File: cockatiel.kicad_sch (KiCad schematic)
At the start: 44 parts

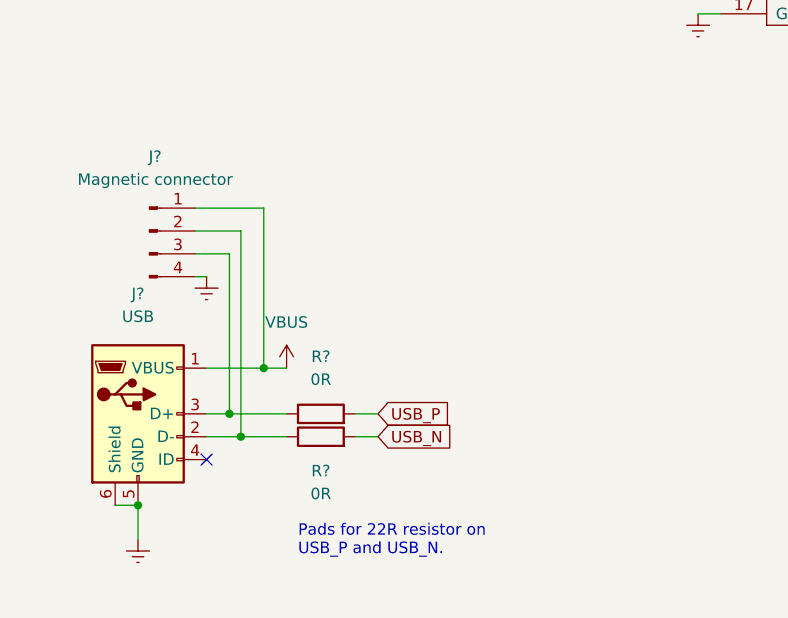
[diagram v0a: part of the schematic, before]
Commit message: Split the USB D+/D- lines using resistors.
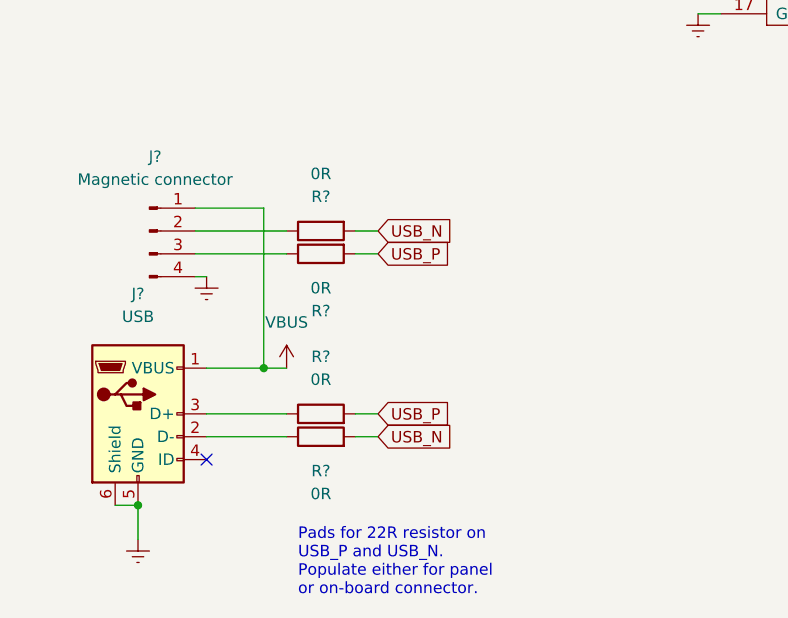
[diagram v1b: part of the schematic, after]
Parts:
- added R? (x2): 0R, Resistor_SMD:R_0805_2012Metric_Pad1.20x1.40mm_HandSolder, symbol Device:R
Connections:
- net USB_N: now also R?.2
- net USB_P: now also R?.2
- net at J?.3 (D+), R?.1: no longer J?.3 (Pin_3)
- net at J?.2 (D-), R?.1: no longer J?.2 (Pin_2)
- new net: J?.2 (Pin_2), R?.1
- new net: J?.3 (Pin_3), R?.1
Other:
- note added: "Pads for 22R resistor on USB_P and USB_N. Populate either for panel or on-board connector."
- note removed: "Pads for 22R resistor on USB_P and USB_N."
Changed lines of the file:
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@@
   (junction (at 212.09 121.92) (diameter 0) (color 0 0 0 0)
   )
-  (junction (at 38.1 176.53) (diameter 0) (color 0 0 0 0)
-  )
   (junction (at 219.71 121.92) (diameter 0) (color 0 0 0 0)
   )
@@
   )
   (junction (at 142.24 186.69) (diameter 0) (color 0 0 0 0)
-  )
-  (junction (at 36.83 173.99) (diameter 0) (color 0 0 0 0)
   )
   (junction (at 142.24 163.83) (diameter 0) (color 0 0 0 0)
@@
     (stroke (width 0) (type default) (color 0 0 0 0))
   )
+  (wire (pts (xy 33.02 153.67) (xy 43.18 153.67))
+    (stroke (width 0) (type default) (color 0 0 0 0))
+  )
   (wire (pts (xy 76.2 52.07) (xy 77.47 52.07))
     (stroke (width 0) (type default) (color 0 0 0 0))
@@
     (stroke (width 0) (type default) (color 0 0 0 0))
   )
+  (wire (pts (xy 50.8 156.21) (xy 53.34 156.21))
+    (stroke (width 0) (type default) (color 0 0 0 0))
+  )
   (wire (pts (xy 211.455 34.925) (xy 211.455 32.385))
     (stroke (width 0) (type default) (color 0 0 0 0))
@@
     (stroke (width 0) (type default) (color 0 0 0 0))
   )
-  (wire (pts (xy 36.83 173.99) (xy 43.18 173.99))
+  (wire (pts (xy 34.29 173.99) (xy 43.18 173.99))
     (stroke (width 0) (type default) (color 0 0 0 0))
   )
@@
     (stroke (width 0) (type default) (color 0 0 0 0))
   )
+  (wire (pts (xy 33.02 156.21) (xy 43.18 156.21))
+    (stroke (width 0) (type default) (color 0 0 0 0))
+  )
   (wire (pts (xy 201.295 34.925) (xy 208.915 34.925))
     (stroke (width 0) (type default) (color 0 0 0 0))
@@
     (stroke (width 0) (type default) (color 0 0 0 0))
   )
+  (wire (pts (xy 50.8 153.67) (xy 53.34 153.67))
+    (stroke (width 0) (type default) (color 0 0 0 0))
+  )
   (wire (pts (xy 235.585 34.925) (xy 235.585 21.59))
     (stroke (width 0) (type default) (color 0 0 0 0))
@@
     (stroke (width 0) (type default) (color 0 0 0 0))
   )
-  (wire (pts (xy 34.29 176.53) (xy 38.1 176.53))
-    (stroke (width 0) (type default) (color 0 0 0 0))
-  )
   (wire (pts (xy 69.85 116.84) (xy 91.44 116.84))
     (stroke (width 0) (type default) (color 0 0 0 0))
@@
     (stroke (width 0) (type default) (color 0 0 0 0))
   )
-  (wire (pts (xy 38.1 176.53) (xy 43.18 176.53))
+  (wire (pts (xy 34.29 176.53) (xy 43.18 176.53))
     (stroke (width 0) (type default) (color 0 0 0 0))
   )
@@
     (stroke (width 0) (type default) (color 0 0 0 0))
   )
-  (wire (pts (xy 33.02 153.67) (xy 38.1 153.67))
-    (stroke (width 0) (type default) (color 0 0 0 0))
-  )
   (wire (pts (xy 267.97 121.92) (xy 267.97 130.81))
     (stroke (width 0) (type default) (color 0 0 0 0))
@@
     (stroke (width 0) (type default) (color 0 0 0 0))
   )
-  (wire (pts (xy 34.29 173.99) (xy 36.83 173.99))
-    (stroke (width 0) (type default) (color 0 0 0 0))
-  )
   (wire (pts (xy 102.87 39.37) (xy 101.6 39.37))
     (stroke (width 0) (type default) (color 0 0 0 0))
@@
     (stroke (width 0) (type default) (color 0 0 0 0))
   )
-  (wire (pts (xy 36.83 156.21) (xy 36.83 173.99))
-    (stroke (width 0) (type default) (color 0 0 0 0))
-  )
   (wire (pts (xy 121.92 189.23) (xy 128.27 189.23))
     (stroke (width 0) (type default) (color 0 0 0 0))
@@
     (stroke (width 0) (type default) (color 0 0 0 0))
   )
-  (wire (pts (xy 33.02 156.21) (xy 36.83 156.21))
-    (stroke (width 0) (type default) (color 0 0 0 0))
-  )
   (wire (pts (xy 143.51 166.37) (xy 146.05 166.37))
     (stroke (width 0) (type default) (color 0 0 0 0))
@@
     (stroke (width 0) (type default) (color 0 0 0 0))
   )
-  (wire (pts (xy 38.1 153.67) (xy 38.1 176.53))
-    (stroke (width 0) (type default) (color 0 0 0 0))
-  )
   (wire (pts (xy 30.48 119.38) (xy 36.83 119.38))
     (stroke (width 0) (type default) (color 0 0 0 0))
@@
     (stroke (width 0) (type default) (color 0 0 0 0))
   )
-  (text "Pads for 22R resistor on \nUSB_P and USB_N." (at 44.45 189.865 0)
+  (text "Pads for 22R resistor on \nUSB_P and USB_N.\nPopulate either for panel\nor on-board connector."
+    (at 44.45 194.31 0)
     (effects (font (size 1.27 1.27)) (justify left bottom))
   )
@@
     )
   )
+  (global_label "USB_N" (shape input) (at 53.34 153.67 0) (fields_autoplaced)
+    (effects (font (size 1.27 1.27)) (justify left))
+    (property "Intersheet References" "${INTERSHEET_REFS}" (id 0) (at 61.8612 153.5906 0)
+      (effects (font (size 1.27 1.27)) (justify left) hide)
+    )
+  )
   (global_label "BT_UART_RX" (shape input) (at 88.9 114.3 180) (fields_autoplaced)
     (effects (font (size 1.27 1.27)) (justify right))
@@
     (property "Intersheet References" "${INTERSHEET_REFS}" (id 0) (at 75.4802 111.6806 0)
       (effects (font (size 1.27 1.27)) (justify right) hide)
+    )
+  )
+  (global_label "USB_P" (shape input) (at 53.34 156.21 0) (fields_autoplaced)
+    (effects (font (size 1.27 1.27)) (justify left))
+    (property "Intersheet References" "${INTERSHEET_REFS}" (id 0) (at 61.8007 156.1306 0)
+      (effects (font (size 1.27 1.27)) (justify left) hide)
     )
   )
@@
     (pin "1")
   )
+  (symbol (lib_id "Device:R") (at 46.99 153.67 90) (mirror x) (unit 1)
+    (in_bom yes) (on_board yes) (fields_autoplaced)
+    (property "Reference" "R?" (id 0) (at 46.99 149.86 90))
+    (property "Value" "0R" (id 1) (at 46.99 147.32 90))
+    (property "Footprint" "Resistor_SMD:R_0805_2012Metric_Pad1.20x1.40mm_HandSolder" (id 2) (at 46.99 151.892 90)
+      (effects (font (size 1.27 1.27)) hide)
+    )
+    (property "Datasheet" "~" (id 3) (at 46.99 153.67 0)
+      (effects (font (size 1.27 1.27)) hide)
+    )
+    (pin "1")
+    (pin "2")
+  )
   (symbol (lib_id "power:Earth") (at 146.05 166.37 0) (unit 1)
     (in_bom yes) (on_board yes) (fields_autoplaced)
@@
     )
     (pin "1")
+  )
+  (symbol (lib_id "Device:R") (at 46.99 156.21 90) (mirror x) (unit 1)
+    (in_bom yes) (on_board yes) (fields_autoplaced)
+    (property "Reference" "R?" (id 0) (at 46.99 162.56 90))
+    (property "Value" "0R" (id 1) (at 46.99 160.02 90))
+    (property "Footprint" "Resistor_SMD:R_0805_2012Metric_Pad1.20x1.40mm_HandSolder" (id 2) (at 46.99 154.432 90)
+      (effects (font (size 1.27 1.27)) hide)
+    )
+    (property "Datasheet" "~" (id 3) (at 46.99 156.21 0)
+      (effects (font (size 1.27 1.27)) hide)
+    )
+    (pin "1")
+    (pin "2")
   )
   (symbol (lib_id "Device:R") (at 82.55 53.34 0) (unit 1)
@@
       (reference "R?") (unit 1) (value "330") (footprint "Resistor_SMD:R_0805_2012Metric_Pad1.20x1.40mm_HandSolder")
     )
+    (path "/8bef48da-1a77-4708-80d6-e40ce0804d8b"
+      (reference "R?") (unit 1) (value "0R") (footprint "Resistor_SMD:R_0805_2012Metric_Pad1.20x1.40mm_HandSolder")
+    )
     (path "/984a861b-f6fe-4e48-b308-c05544ae2128"
       (reference "R?") (unit 1) (value "2K2") (footprint "")
@@
       (reference "R?") (unit 1) (value "330") (footprint "Resistor_SMD:R_0805_2012Metric_Pad1.20x1.40mm_HandSolder")
     )
+    (path "/b804d89b-7db6-4577-a13e-be600d5ceaab"
+      (reference "R?") (unit 1) (value "0R") (footprint "Resistor_SMD:R_0805_2012Metric_Pad1.20x1.40mm_HandSolder")
+    )
     (path "/bb6848f3-ae47-41fd-84f7-dda98b97154e"

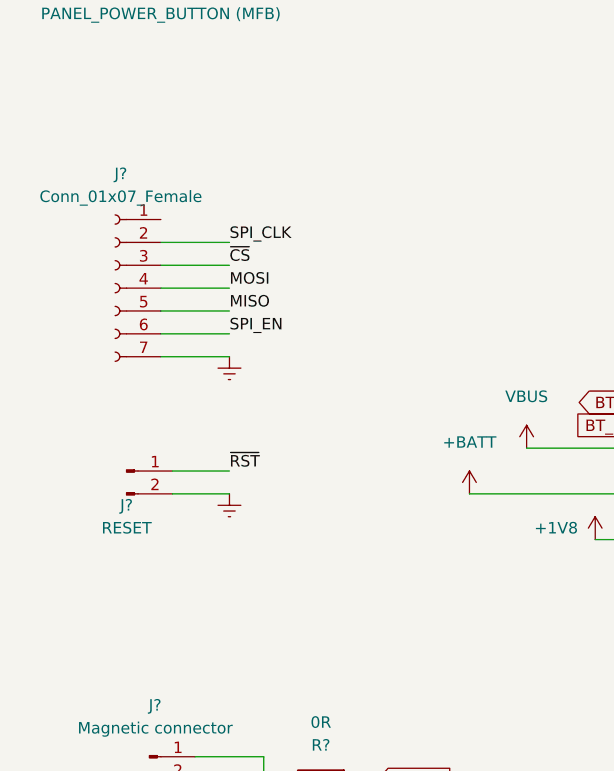
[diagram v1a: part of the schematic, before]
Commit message: Bring out the debug UART to a jumper
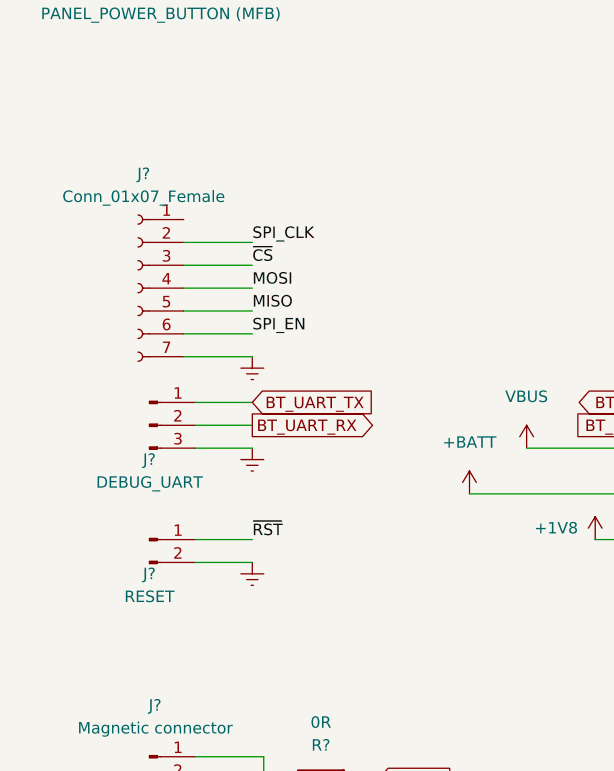
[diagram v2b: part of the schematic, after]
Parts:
- added J?: DEBUG_UART, Connector_PinHeader_2.54mm:PinHeader_1x03_P2.54mm_Vertical, symbol Connector:Conn_01x03_Male
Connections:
- net BT_UART_RX: now also J?.2 (Pin_2)
- net BT_UART_TX: now also J?.1 (Pin_1)
- net Earth: now also J?.3 (Pin_3)
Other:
- moved on the sheet: J?

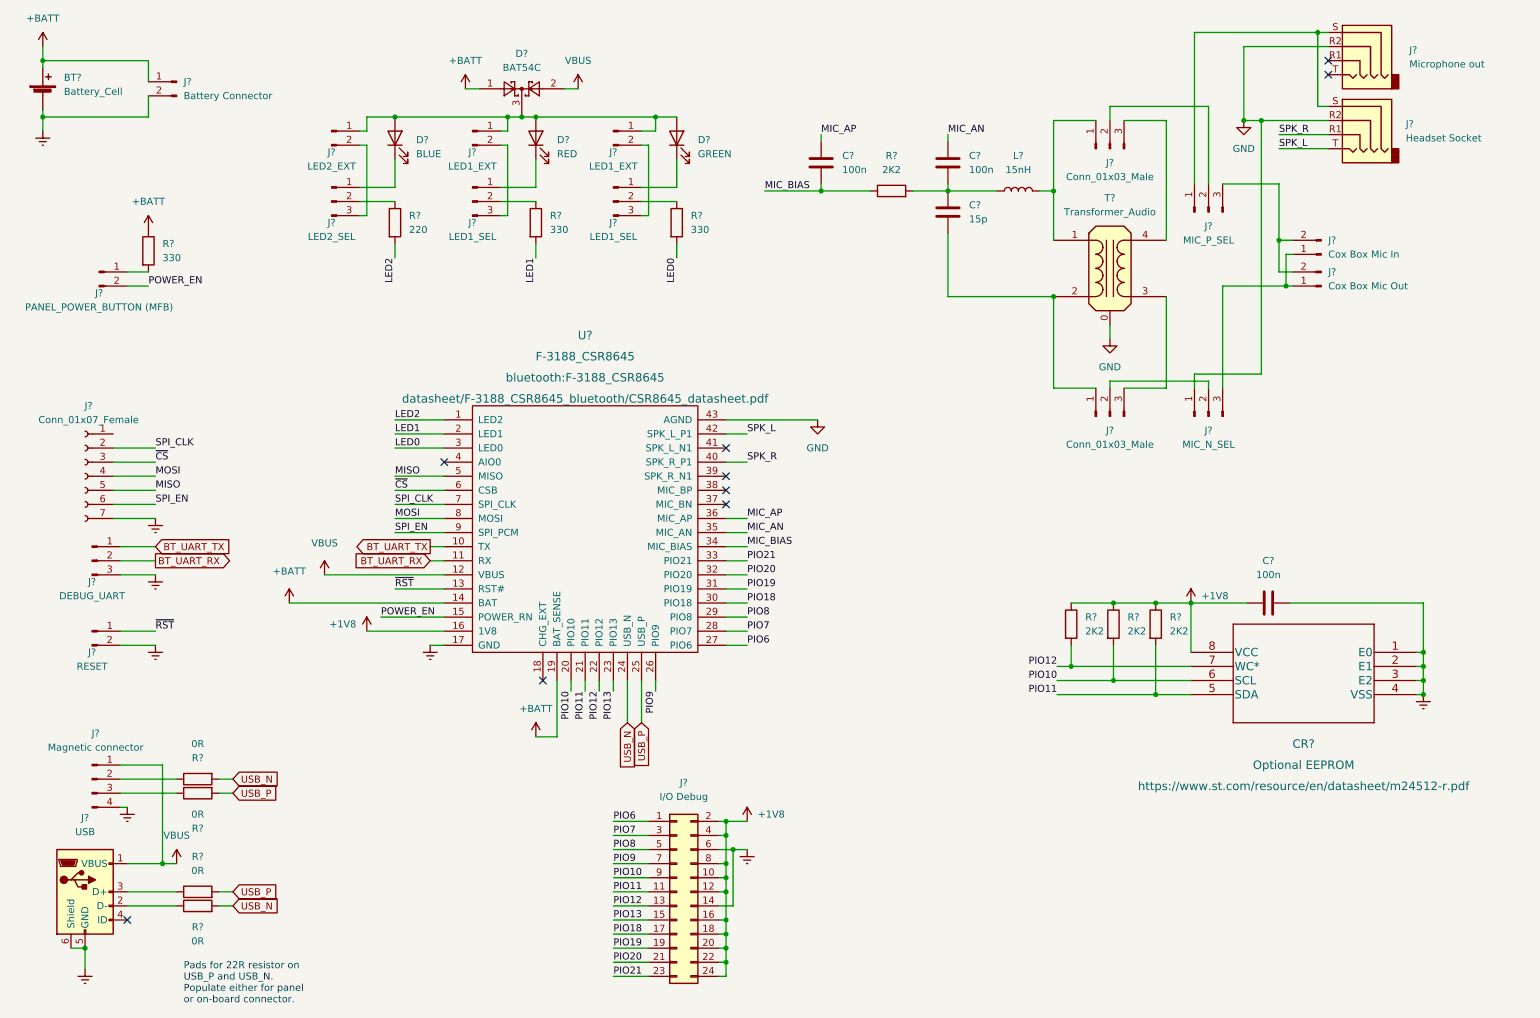
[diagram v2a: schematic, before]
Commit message: Initial work on the board layout
This includes assigning some LCSC parts for use with JLCPCB.
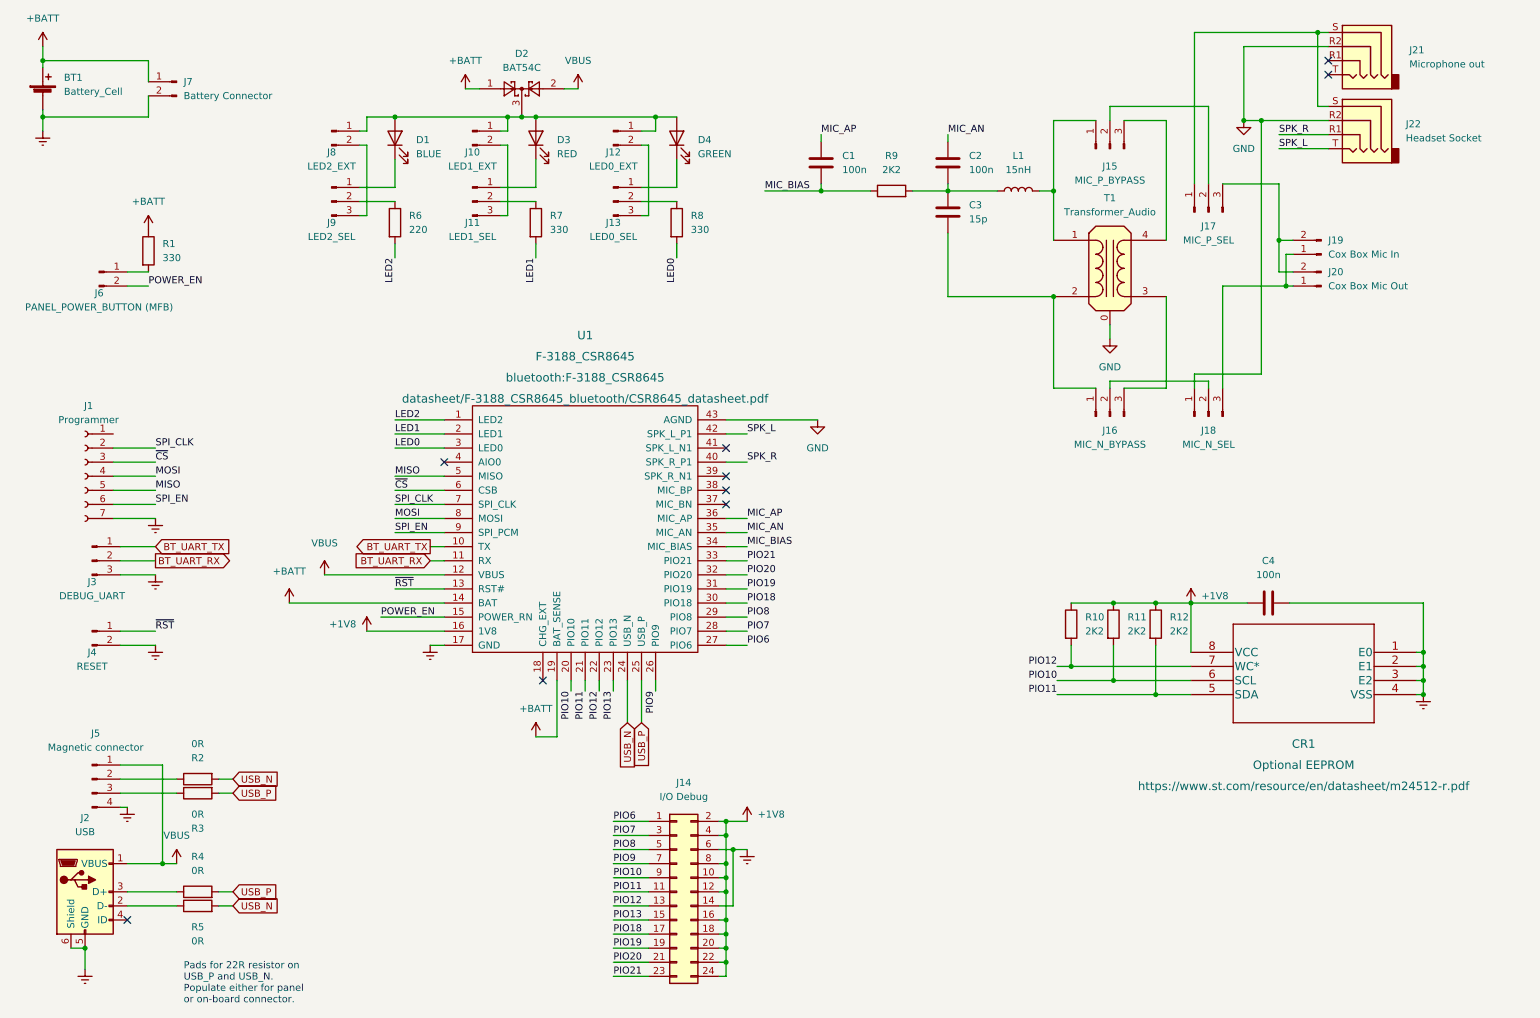
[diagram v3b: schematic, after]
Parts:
- D2: renamed from D?; LCSC (none) -> C37704
- J1: renamed from J?; value Conn_01x07_Female -> Programmer
- J10, J19, J20, J6, J8: renamed from J?; LCSC (none) -> C492401
- J11, J17, J18, J3, J4, J9: renamed from J?; LCSC (none) -> C49257
- J12: renamed from J?; value LED1_EXT -> LED0_EXT; LCSC (none) -> C492401
- J13: renamed from J?; value LED1_SEL -> LED0_SEL; LCSC (none) -> C49257
- J15: renamed from J?; value Conn_01x03_Male -> MIC_P_BYPASS; LCSC (none) -> C49257
- J16: renamed from J?; value Conn_01x03_Male -> MIC_N_BYPASS; LCSC (none) -> C49257
- gave numbers to parts that had none: 30
